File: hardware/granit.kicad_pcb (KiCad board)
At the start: 4 copper layers, 92 x 100 mm, 108 parts, among them IC1 ASM1061, J1 12V Barrel, J2 12V Screw Terminal, J3 RJ45_RB1-125B8G1A, J6 Conn_01x02, J7 USB_C_Receptacle_USB2.0_14P, J8 Conn_01x03, J9 SATA_22pin, Q1 FDS4435BZ, Q2 FDS4435BZ, Q3 FDS4435BZ, Q4 2N7002, Q5 2N7002, Q6 2N7002, SW1 SW_Push, U1 NCP1117-3.3_SOT223, U2 AP64501SP-13, U3 74AHCT1G125, U4 DS3231MZ, U5 USBLC6-2SC6, U6 74AHCT1G32, Y1 Crystal

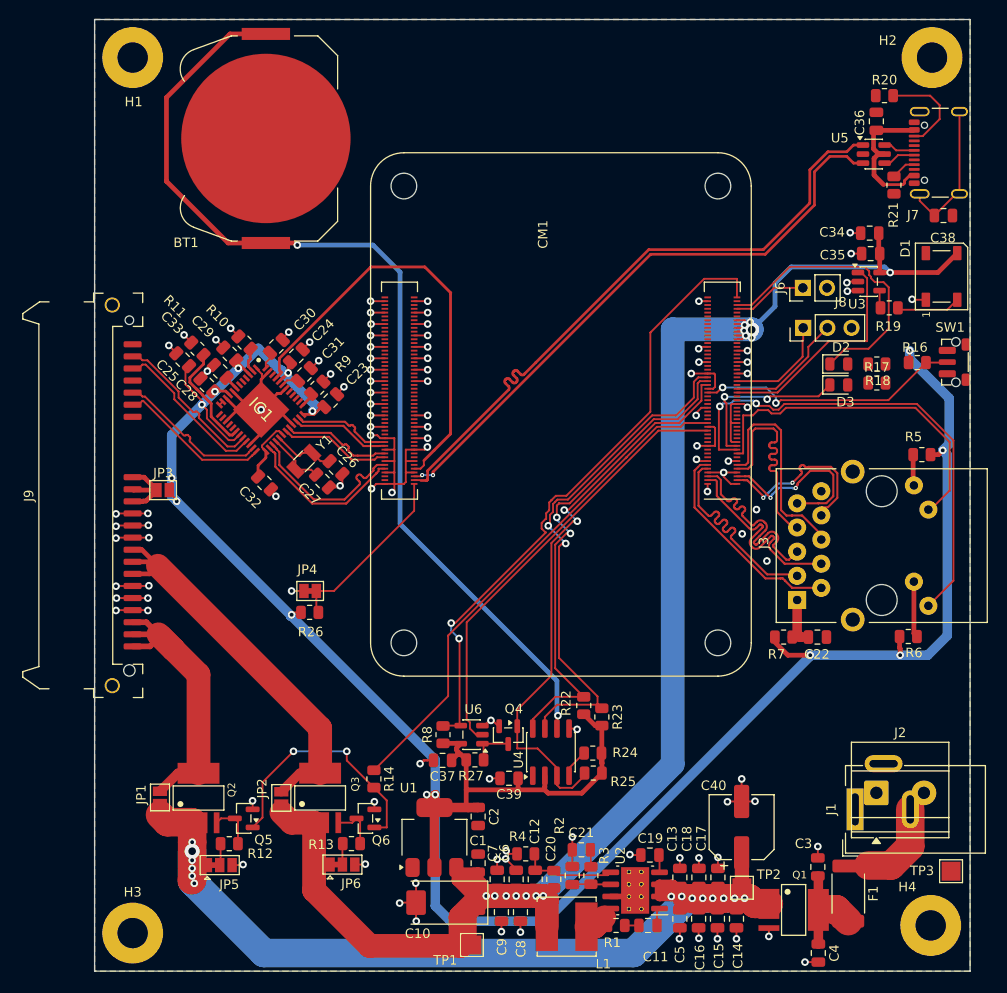
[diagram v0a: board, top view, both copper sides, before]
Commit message: Place fiducials, continue routing
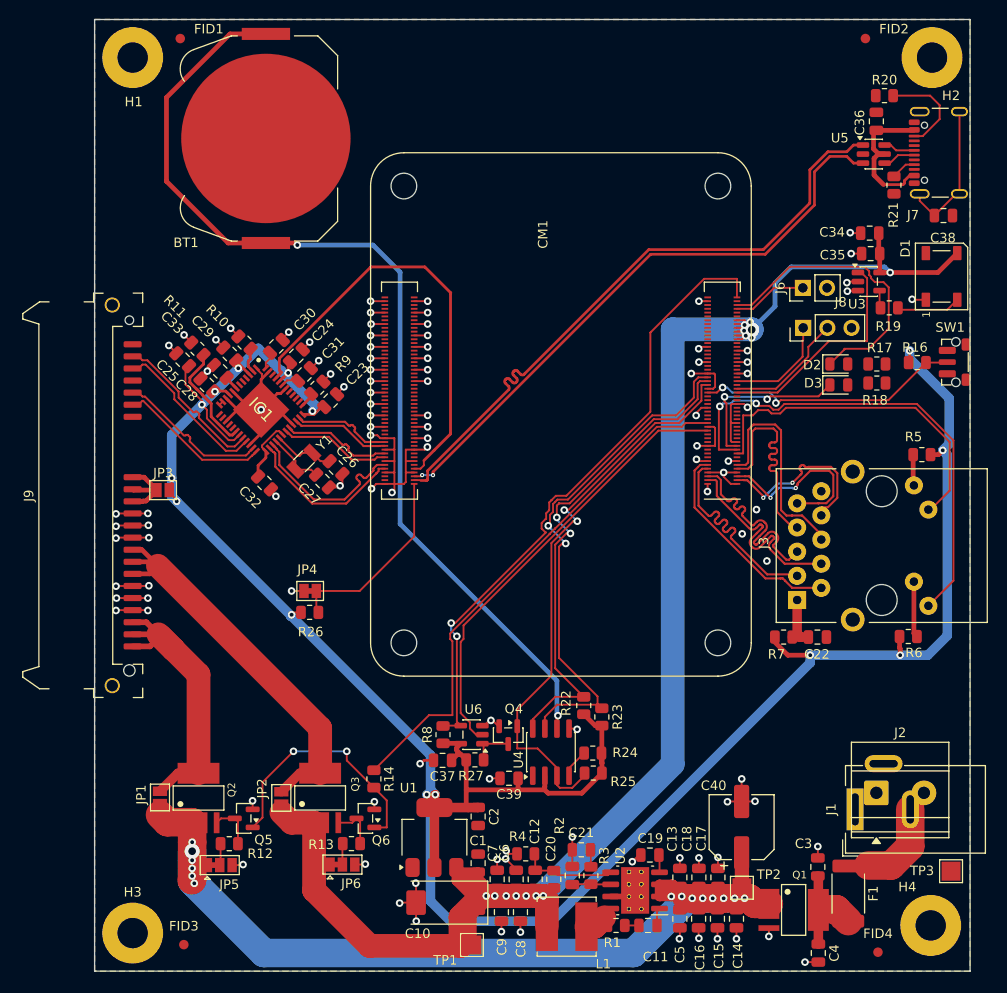
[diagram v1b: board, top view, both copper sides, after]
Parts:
- added FID1: Fiducial, Fiducial:Fiducial_1mm_Mask2mm, F.Cu at (29.0, 22.0)
- added FID2: Fiducial, Fiducial:Fiducial_1mm_Mask2mm, F.Cu at (101.0, 22.0)
- added FID3: Fiducial, Fiducial:Fiducial_1mm_Mask2mm, F.Cu at (29.4, 117.2)
- added FID4: Fiducial, Fiducial:Fiducial_1mm_Mask2mm, F.Cu at (102.3, 118.0)
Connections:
- CM1 pad 30: SATA_PWR_EN -> GPIO_HOLD
- CM1 pad 34: GPIO_HOLD -> SATA_PWR_EN
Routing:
- net GND: track 203.7 -> 194.7 mm
- net +3V3: track 266.0 -> 263.8 mm
- net SATA_PWR_EN: track 54.1 -> 55.6 mm
- net USB_OTG_ID: track 18.9 -> 20.2 mm
- net RTC_INT: track 60.7 -> 59.6 mm
- net Net-(U4-~{RST}): track 3.03 -> 2.24 mm
- net SDA1: track 56.0 -> 55.5 mm

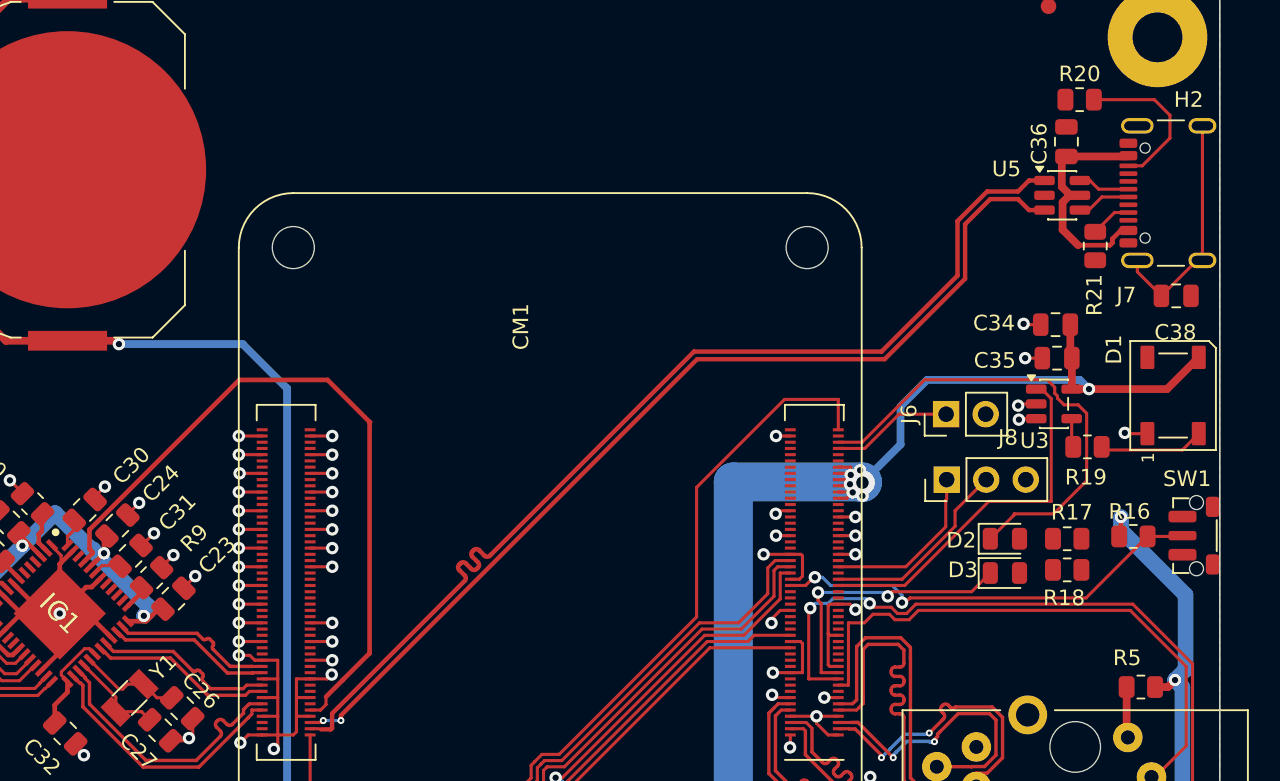
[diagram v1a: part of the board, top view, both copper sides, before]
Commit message: Route USB-C, LEDs, button, peripherals — 4 unconnected remaining
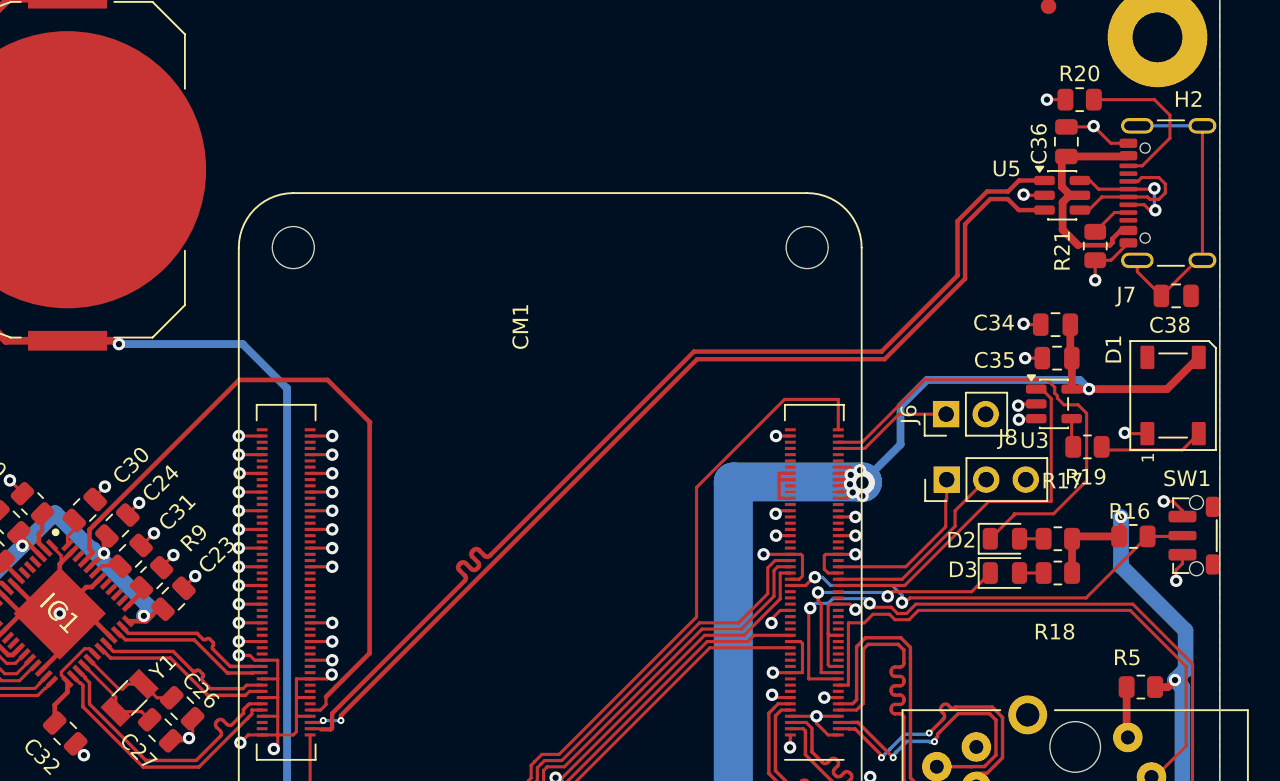
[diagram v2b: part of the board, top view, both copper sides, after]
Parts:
- moved R18 2.28 mm to (101.6, 58.4)
- moved R17 2.09 mm to (101.6, 56.2)
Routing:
- net GND: track 194.7 -> 212.0 mm, vias 106 -> 112
- net Net-(J7-D+-PadA6): track 3.46 -> 9.29 mm
- net +3V3: track 263.8 -> 269.1 mm
- net Net-(J7-D--PadA7): track 3.34 -> 8.34 mm, vias 0 -> 2
- net Net-(J7-SHIELD): track 14.8 -> 19.0 mm
- net Net-(CM1A-GPIO_VREF(1.8v/3.3v_Input)): track 0.00 -> 3.76 mm
- net Net-(D3-A): track 0.00 -> 1.55 mm
- net Net-(D2-A): track 0.00 -> 1.55 mm

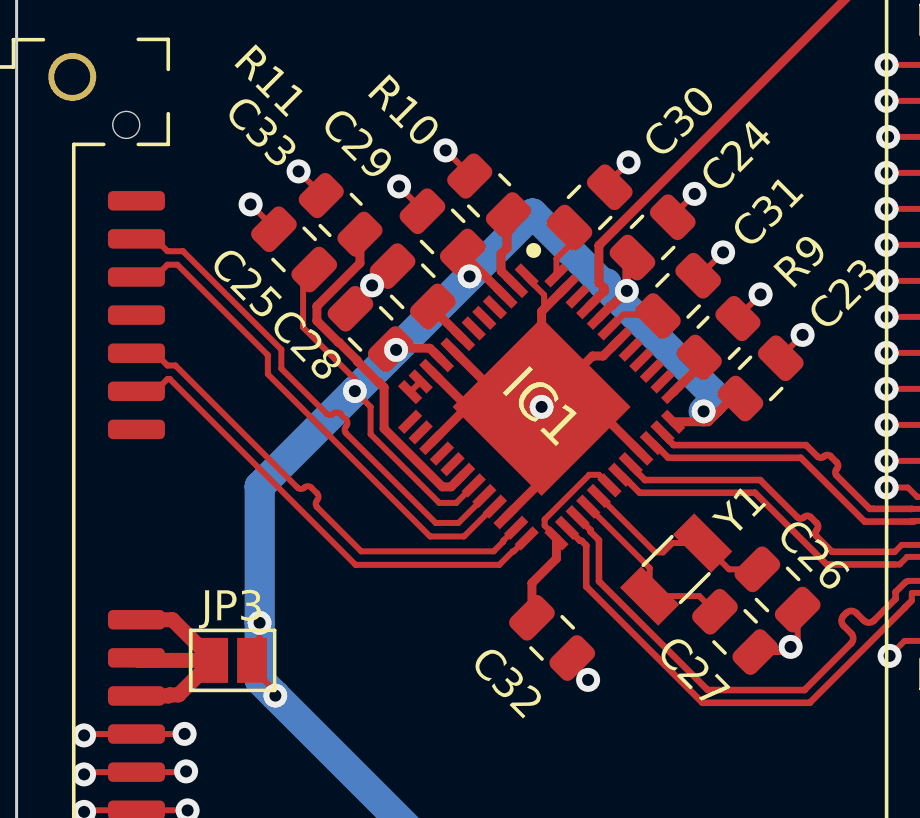
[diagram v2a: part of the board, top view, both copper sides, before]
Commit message: Complete routing — zero unconnected nets
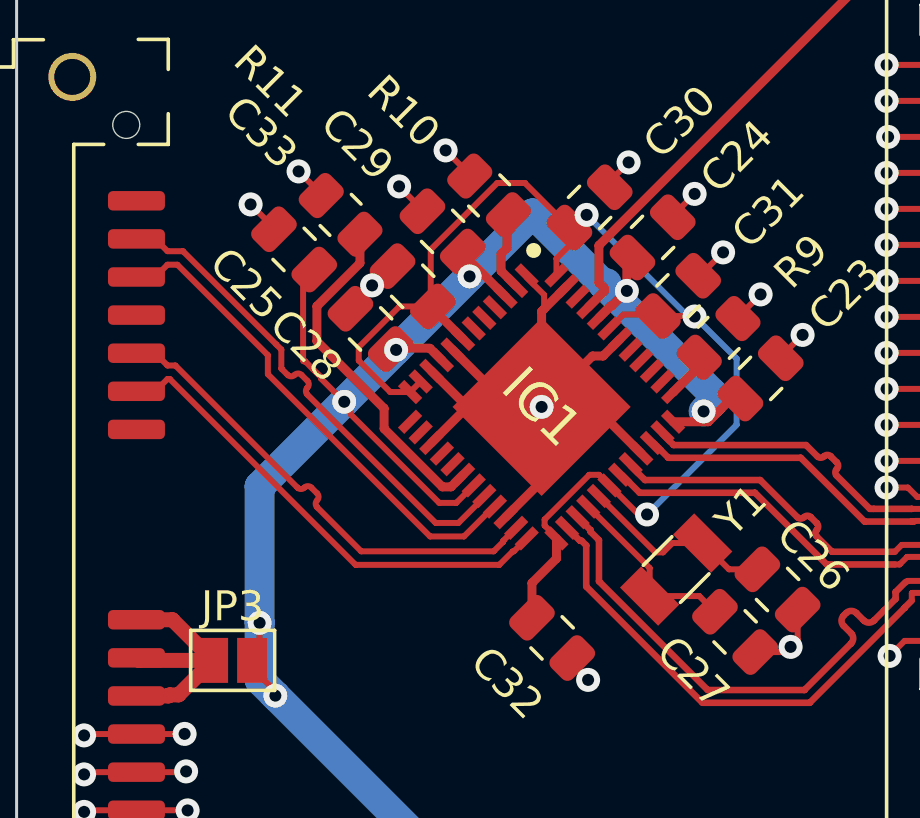
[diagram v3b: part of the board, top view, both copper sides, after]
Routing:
- net Net-(IC1-VCC12_1): track 11.9 -> 42.7 mm, vias 0 -> 3

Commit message: Update footprints from library
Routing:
- net +5VP: vias 14 -> 12
